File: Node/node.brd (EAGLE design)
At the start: 76.2 x 25.4 mm, 96 parts, among them CN4 MicroUSB, J1 U.FL, U1 MCP73871, U2 DW1000-I, U3 TPS61090RSAR, U4 ATMEGA328, X2 332-02, Y1 8MHz

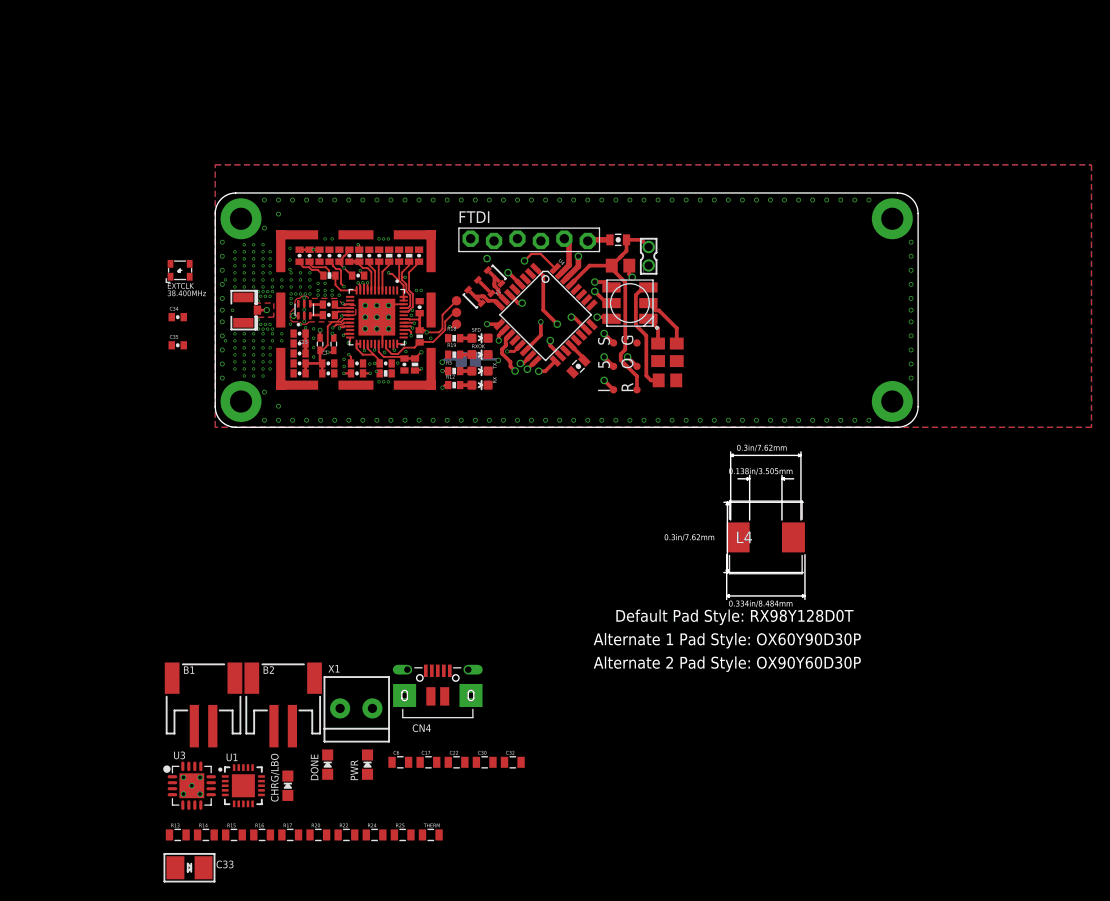
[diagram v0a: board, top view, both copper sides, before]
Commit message: More RF work. Increased the RF shield size, routed TCXO.
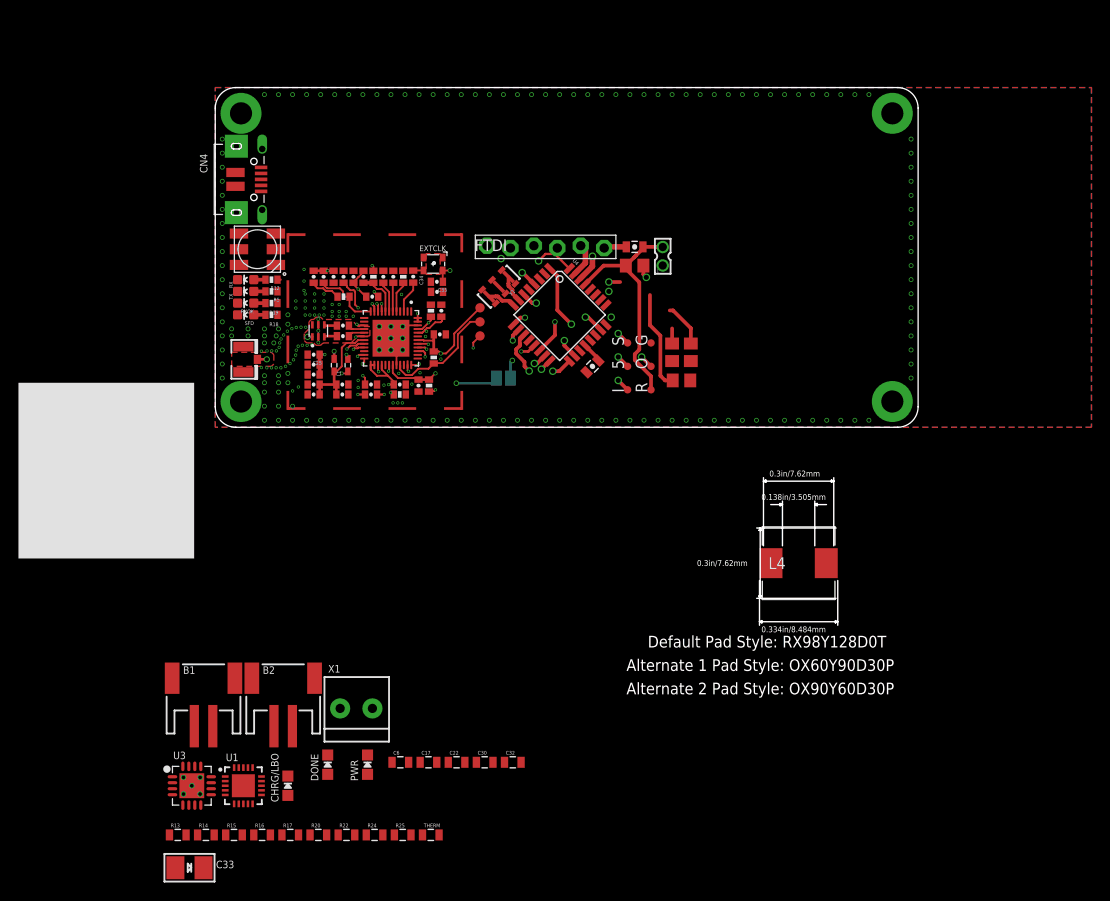
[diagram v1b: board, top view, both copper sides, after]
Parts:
- removed U$1: 5BMI-S-202-F, MainLib:BMI-S-102
- added U$6: SMS-255F, MainLib:SMS-255F
- moved CN4 57.6 mm to (4.19, 26.9), turned to 270 degrees
- moved LED1 40.8 mm to (4.57, 19.3)
- moved C35 28.9 mm to (24.0, 15.8)
- moved RX 27.9 mm to (3.30, 16.0), turned to 90 degrees
- moved EXTCLK 27.4 mm to (23.6, 17.7), turned to 180 degrees
- moved TX 26.8 mm to (3.30, 14.7), turned to 90 degrees
- moved RXOK 26.0 mm to (3.30, 13.5), turned to 90 degrees
- moved C34 25.9 mm to (21.5, 16.3), turned to 90 degrees
- moved SFD 25.5 mm to (3.30, 12.2), turned to 90 degrees
- moved R12 22.9 mm to (6.10, 16.0), turned to 180 degrees
- moved R5 21.6 mm to (6.10, 14.7), turned to 180 degrees
- moved R19 20.6 mm to (6.10, 13.5), turned to 180 degrees
- moved R18 20.0 mm to (6.10, 12.2), turned to 180 degrees
- moved C5 6.44 mm to (24.5, 12.6)
- moved R7 6.42 mm to (23.4, 12.6)
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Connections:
- net GND: now also U$6.P$1, U$6.P$10, U$6.P$11, U$6.P$12, U$6.P$13, U$6.P$14, U$6.P$15, U$6.P$16, U$6.P$2, U$6.P$3, U$6.P$4, U$6.P$5, U$6.P$6, U$6.P$7, U$6.P$8, U$6.P$9; no longer U$1.P$1, U$1.P$10, U$1.P$11, U$1.P$12, U$1.P$2, U$1.P$3, U$1.P$4, U$1.P$5, U$1.P$6, U$1.P$7, U$1.P$8, U$1.P$9
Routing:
- net IQR: track 29.1 -> 23.0 mm
- net GPIO3: track 11.8 -> 6.97 mm, vias 2 -> 1
- net GPIO2: track 9.50 -> 5.03 mm, vias 2 -> 1
- net N$25: track 0.00 -> 3.55 mm
- net GRN: track 27.2 -> 23.7 mm
- net N$10: track 23.2 -> 20.1 mm
- net 3.3V: track 23.7 -> 20.7 mm, vias 11 -> 12
- net !RST: track 13.1 -> 15.4 mm
- net ANT: track 4.68 -> 6.96 mm
- net GPIO5: track 11.0 -> 12.8 mm
- net RED: track 27.2 -> 25.4 mm
- net GPIO6: track 14.8 -> 16.6 mm
- net N$3: track 12.5 -> 10.8 mm
- net VDDIO: track 19.4 -> 20.9 mm
- net N$4: track 3.12 -> 1.64 mm
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- removed copper zone on layer 15, net ANT
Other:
- board size 76.2 x 25.4 mm -> 76.2 x 36.8 mm

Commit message: Added RF exposed plane to the stop layers as well
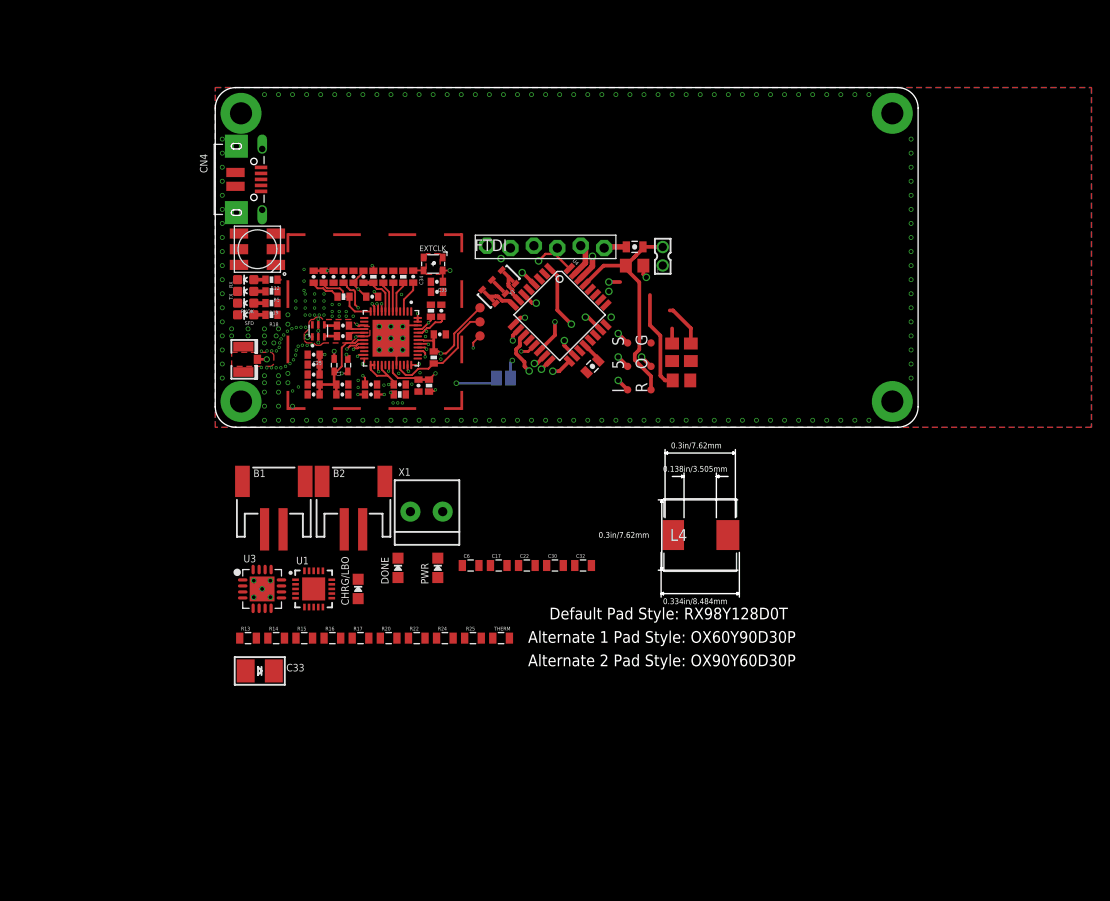
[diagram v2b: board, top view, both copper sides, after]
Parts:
- moved B1 22.7 mm to (6.35, -7.37)
- moved B2 22.7 mm to (15.0, -7.37)
- moved C17 22.7 mm to (30.7, -15.0)
- moved C22 22.7 mm to (33.8, -15.0)
- moved C30 22.7 mm to (36.8, -15.0)
- moved C32 22.7 mm to (39.9, -15.0)
- moved C33 22.7 mm to (4.83, -26.4)
- moved C6 22.7 mm to (27.7, -15.0)
- moved CHRG/LBO 22.7 mm to (15.5, -17.5)
- moved U1 22.7 mm to (10.7, -17.5)
- moved U3 22.7 mm to (5.08, -17.5)
- moved DONE 22.7 mm to (19.8, -15.2)
- moved PWR 22.7 mm to (24.1, -15.2)
- moved R13 22.7 mm to (3.56, -22.9)
- moved R14 22.7 mm to (6.60, -22.9)
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
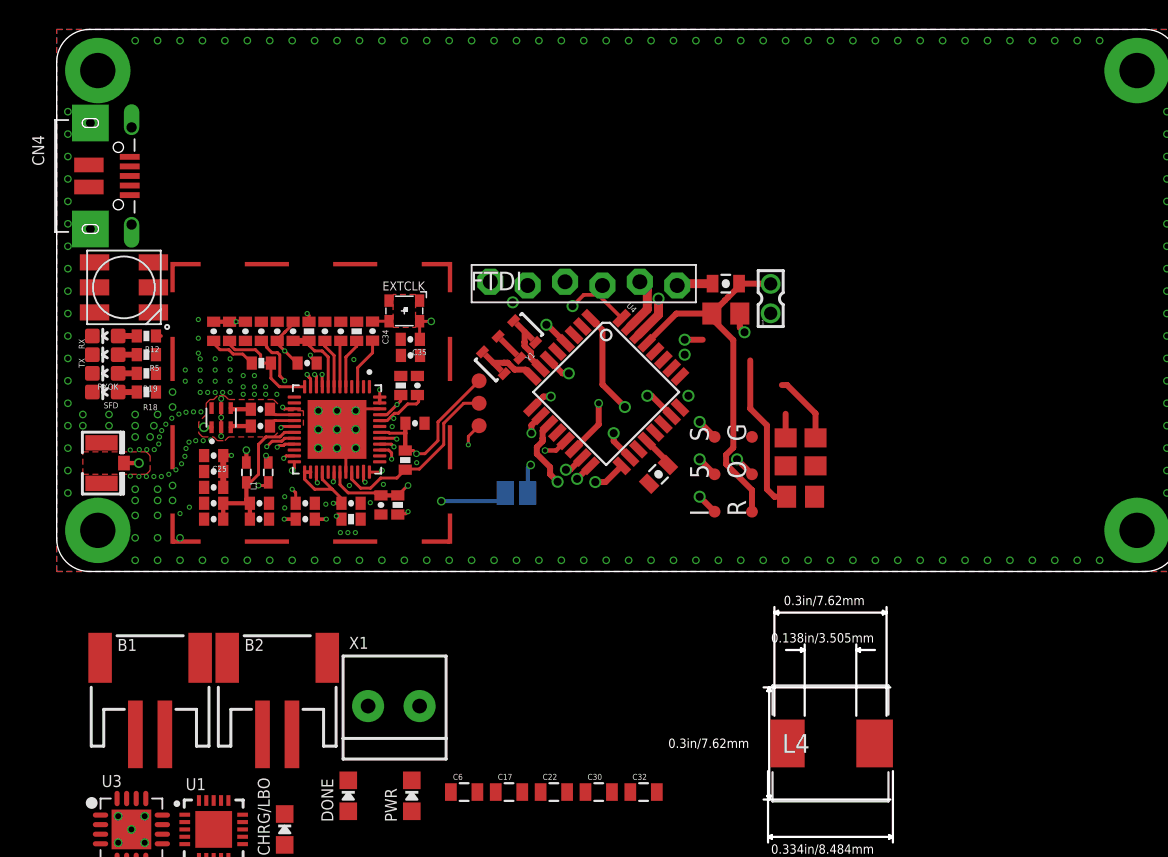
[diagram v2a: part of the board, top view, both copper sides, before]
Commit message: Removed unneeded JST connector
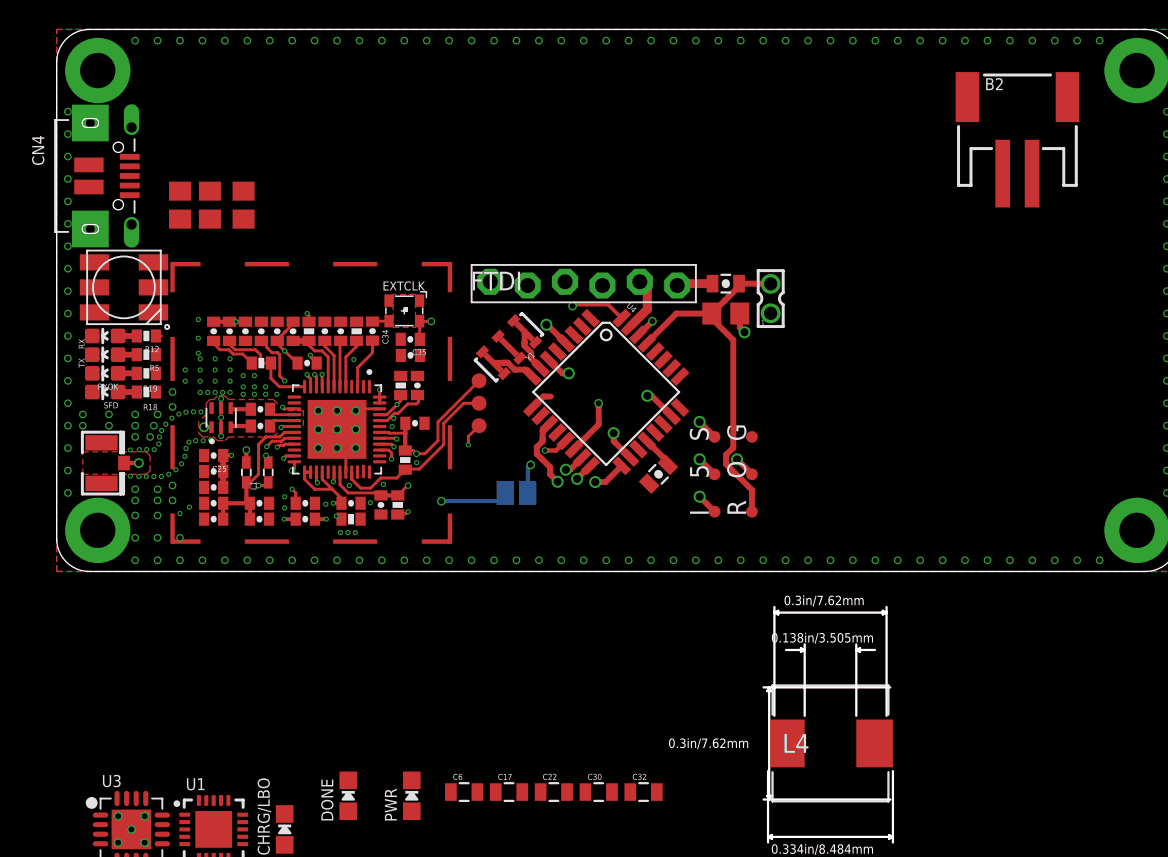
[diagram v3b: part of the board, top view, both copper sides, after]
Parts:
- removed B1: 1.8-5V, microbuilder:JSTPH2
- removed X1: (no value), microbuilder:TERMBLOCK_1X2-3.5MM
- moved B2 63.1 mm to (65.3, 30.7)
- moved R3 44.4 mm to (8.38, 24.9)
- moved R1 44.4 mm to (10.4, 24.9)
- moved R2 42.7 mm to (12.7, 24.9), turned to 90 degrees
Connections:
- net 3.3V: no longer X1.2
- net GND: no longer B1.1, X1.1
- net VBAT: no longer B1.2
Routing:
- net RED: track 25.4 -> 0.54 mm, vias 2 -> 0
- net GRN: track 23.7 -> 1.57 mm, vias 3 -> 0
- net BLU: track 11.9 -> 0.25 mm, vias 2 -> 0
- net N$3: track 10.8 -> 0.00 mm
- net GPIO3: track 6.97 -> 0.00 mm, vias 1 -> 0
- net N$2: track 4.74 -> 0.00 mm
- net GPIO2: track 5.03 -> 0.34 mm, vias 1 -> 0
- net N$4: track 1.64 -> 0.00 mm
- net RXD: track 7.43 -> 6.29 mm
- net IQR: track 23.0 -> 22.5 mm

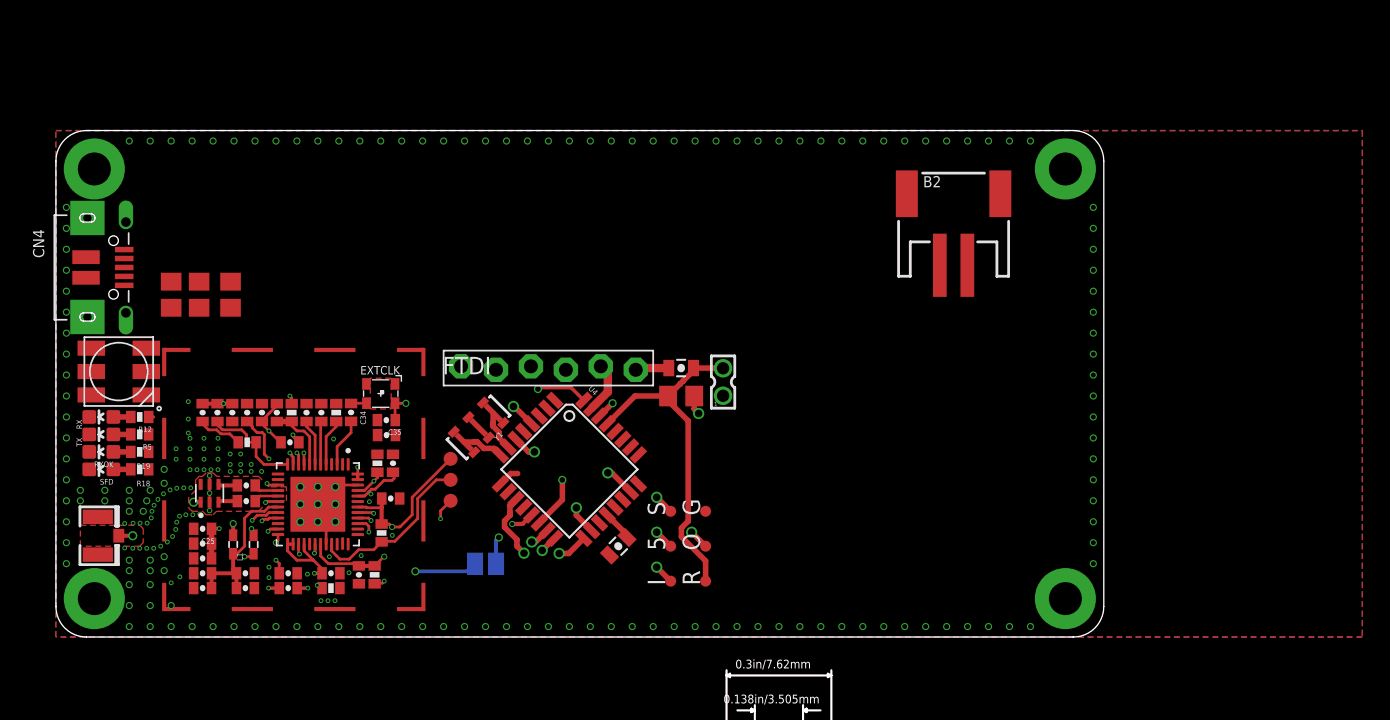
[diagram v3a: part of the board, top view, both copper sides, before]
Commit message: Routed LEDs near side wall. Changed overall size. Added heatsink. Created an exposed-copper version of the logo.
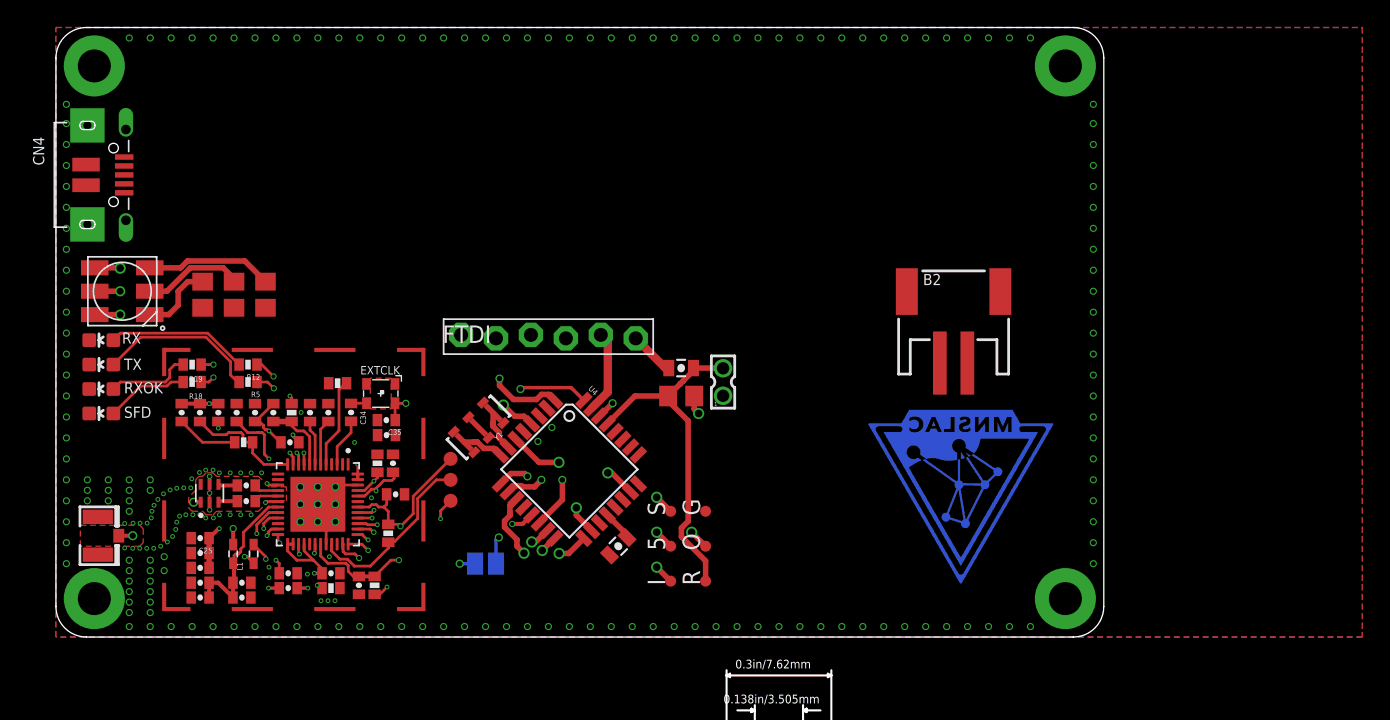
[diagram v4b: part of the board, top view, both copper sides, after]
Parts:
- added U$1: MNSLAC0.25-EXP, MainLib:MNSLAC-0.25-EXPOSED
- added U$7: HEATSINK, MainLib:LTN20069
- moved R12 8.75 mm to (14.0, 19.8)
- moved R5 8.75 mm to (14.0, 18.5)
- moved R18 7.41 mm to (9.91, 18.5)
- moved R19 7.41 mm to (9.91, 19.8)
- moved B2 7.11 mm to (65.3, 23.6)
- moved CN4 6.73 mm to (4.19, 33.6)
- moved LED1 5.85 mm to (4.83, 25.1)
- moved RX 5.59 mm to (3.30, 21.6)
- moved TX 5.08 mm to (3.30, 19.8)
- moved RXOK 4.57 mm to (3.30, 18.0)
- moved SFD 4.06 mm to (3.30, 16.3)
- moved R1 2.54 mm to (13.0, 24.9)
- moved R2 2.54 mm to (15.2, 24.9)
- moved FTDI 2.29 mm to (35.8, 21.8)
- moved R3 2.29 mm to (10.7, 24.9)
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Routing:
- net RED: track 0.54 -> 54.0 mm, vias 0 -> 2
- net GRN: track 1.57 -> 49.3 mm, vias 0 -> 2
- net BLU: track 0.25 -> 41.1 mm, vias 0 -> 2
- net GPIO1: track 0.00 -> 24.0 mm, vias 0 -> 2
- net GPIO0: track 0.00 -> 24.0 mm, vias 0 -> 2
- net GPIO3: track 0.00 -> 21.5 mm, vias 0 -> 2
- net GPIO2: track 0.34 -> 21.2 mm, vias 0 -> 2
- net N$5: track 1.27 -> 11.9 mm
- net N$3: track 0.00 -> 9.24 mm
- net N$6: track 1.27 -> 10.3 mm
- net N$2: track 0.00 -> 7.38 mm
- net N$4: track 0.00 -> 5.43 mm
- net N$24: track 1.27 -> 6.16 mm
- net N$21: track 1.27 -> 6.02 mm
- net 3.3V: track 20.7 -> 25.0 mm
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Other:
- board size 76.2 x 36.8 mm -> 76.2 x 44.3 mm
